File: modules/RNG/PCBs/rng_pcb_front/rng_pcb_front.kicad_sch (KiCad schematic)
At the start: 34 parts, among them J1 THONKICONN, J10 Conn_01x08_Pin, J2 THONKICONN, J3 THONKICONN, J4 THONKICONN, J5 THONKICONN, J6 THONKICONN, J7 Conn_01x07_Pin, J8 Conn_02x03_Socket, J9 Conn_01x06_Pin, SW1 RotaryEncoder_Switch, SW2 TAIWAY 200CWMSP1T3B4M2, SW3 TAIWAY 200CWMSP1T3B4M2

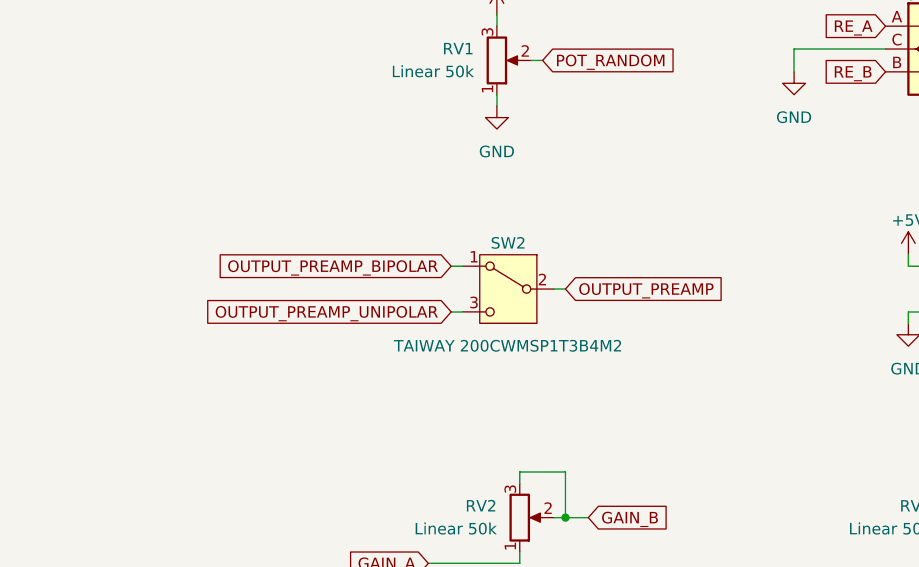
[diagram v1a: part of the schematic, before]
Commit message: update RNG firmware to use new pins
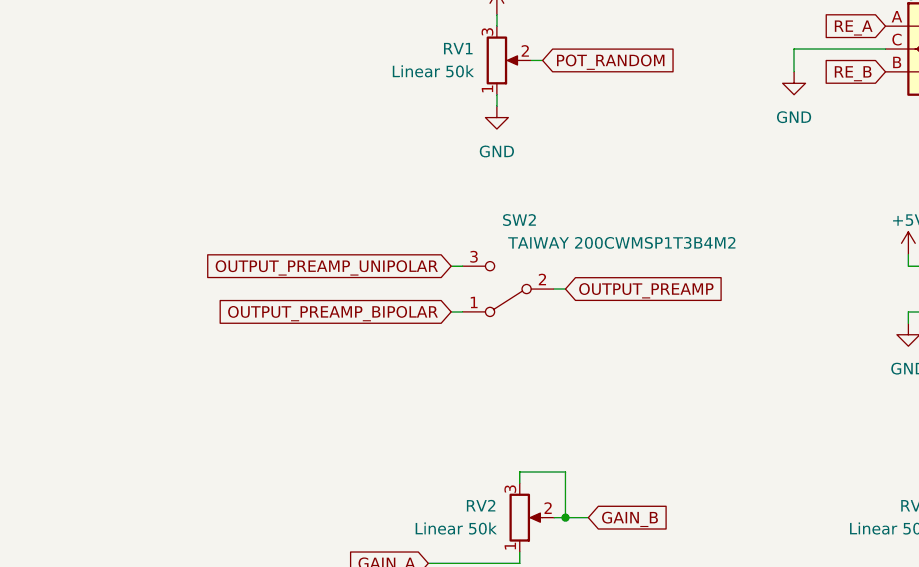
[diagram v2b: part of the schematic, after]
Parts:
- removed SW2: TAIWAY 200CWMSP1T3B4M2, FreeModualr:TAIWAY 200CWMSP1T3B4M2, symbol Switch:SW_SPDT
- added SW2: TAIWAY 200CWMSP1T3B4M2, FreeModualr:TAIWAY 200CWMSP1T3B4M2, symbol FreeModular:SW_SPDT_small
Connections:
- net OUTPUT_PREAMP: now also SW2.2 (B)
- net OUTPUT_PREAMP_BIPOLAR: now also SW2.1 (A)
- net OUTPUT_PREAMP_UNIPOLAR: now also SW2.3 (C)
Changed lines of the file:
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@@
 	(global_label "OUTPUT_PREAMP_UNIPOLAR"
 		(shape input)
-		(at 92.71 106.68 180)
+		(at 92.71 101.6 180)
 		(fields_autoplaced yes)
 		(effects
@@
 		)
 		(property "Intersheetrefs" "${INTERSHEET_REFS}"
-			(at 63.8409 106.68 0)
+			(at 63.8409 101.6 0)
 			(effects
 				(font
@@
 	(global_label "OUTPUT_PREAMP_BIPOLAR"
 		(shape input)
-		(at 92.71 101.6 180)
+		(at 92.71 106.68 180)
 		(fields_autoplaced yes)
 		(effects
@@
 		)
 		(property "Intersheetrefs" "${INTERSHEET_REFS}"
-			(at 65.2319 101.6 0)
+			(at 65.2319 106.68 0)
 			(effects
 				(font
@@
 	)
 	(symbol
+		(lib_id "FreeModular:SW_SPDT_small")
+		(at 99.06 104.14 180)
+		(unit 1)
+		(exclude_from_sim no)
+		(in_bom yes)
+		(on_board yes)
+		(dnp no)
+		(property "Reference" "SW2"
+			(at 100.33 96.52 0)
+			(effects
+				(font
+					(size 1.27 1.27)
+				)
+			)
+		)
+		(property "Value" "TAIWAY 200CWMSP1T3B4M2"
+			(at 111.76 99.06 0)
+			(effects
+				(font
+					(size 1.27 1.27)
+				)
+			)
+		)
+		(property "Footprint" "FreeModualr:TAIWAY 200CWMSP1T3B4M2"
+			(at 99.06 104.14 0)
+			(effects
+				(font
+					(size 1.27 1.27)
+				)
+				(hide yes)
+			)
+		)
+		(property "Datasheet" "https://www.taiway.com/resource/annexes/product_items/81/383d79ce24fd13ac9c4d36337853e90c.pdf"
+			(at 99.06 104.14 0)
+			(effects
+				(font
+					(size 1.27 1.27)
+				)
+				(hide yes)
+			)
+		)
+		(property "Description" ""
+			(at 99.06 104.14 0)
+			(effects
+				(font
+					(size 1.27 1.27)
+				)
+				(hide yes)
+			)
+		)
+		(pin "1"
+		)
+		(pin "2"
+		)
+		(pin "3"
+		)
+		(instances
+			(project "rng_pcb_front"
+				(path "/53c2a808-e337-4b11-8126-cc5e1b54736a"
+					(reference "SW2")
+					(unit 1)
+				)
+			)
+		)
+	)
+	(symbol
 		(lib_id "Device:R")
 		(at 246.38 102.87 90)
@@
 					(unit 1)
 				)
-			)
-		)
-	)
-	(symbol
-		(lib_id "Switch:SW_SPDT")
-		(at 99.06 104.14 0)
-		(mirror y)
-		(unit 1)
-		(exclude_from_sim no)
-		(in_bom yes)
-		(on_board yes)
-		(dnp no)
-		(property "Reference" "SW2"
-			(at 99.06 99.06 0)
-			(effects
-				(font
-					(size 1.27 1.27)
-				)
-			)
-		)
-		(property "Value" "TAIWAY 200CWMSP1T3B4M2"
-			(at 99.06 110.49 0)
-			(effects
-				(font
-					(size 1.27 1.27)
-				)
-			)
-		)
-		(property "Footprint" "FreeModualr:TAIWAY 200CWMSP1T3B4M2"
-			(at 99.06 104.14 0)
-			(effects
-				(font
-					(size 1.27 1.27)
-				)
-				(hide yes)
-			)
-		)
-		(property "Datasheet" "~"
-			(at 99.06 111.76 0)
-			(effects
-				(font
-					(size 1.27 1.27)
-				)
-				(hide yes)
-			)
-		)
-		(property "Description" ""
-			(at 99.06 104.14 0)
-			(effects
-				(font
-					(size 1.27 1.27)
-				)
-				(hide yes)
-			)
-		)
-		(pin "1"
-		)
-		(pin "2"
-		)
-		(pin "3"
-		)
-		(instances
-			(project "rng_pcb_front"
-				(path "/53c2a808-e337-4b11-8126-cc5e1b54736a"
-					(reference "SW2")
-					(unit 1)
-				)

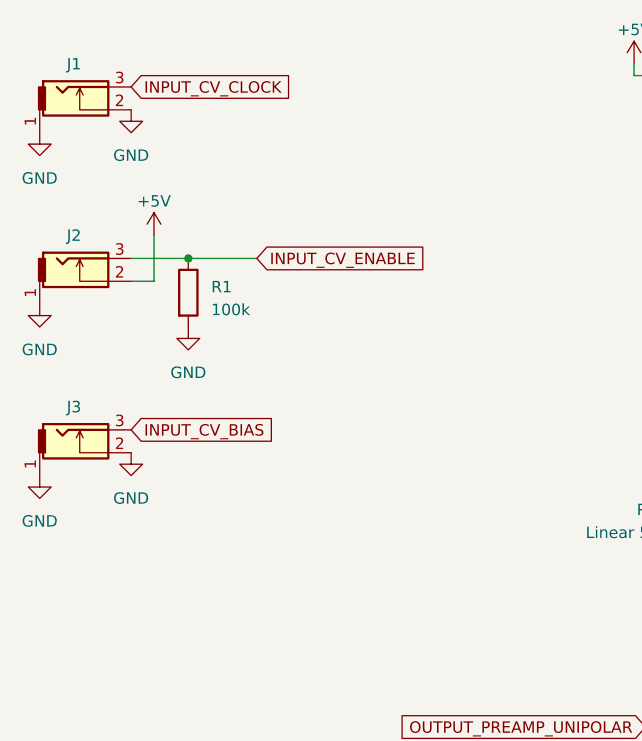
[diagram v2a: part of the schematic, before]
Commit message: add pulldown resistor to RNG clock input
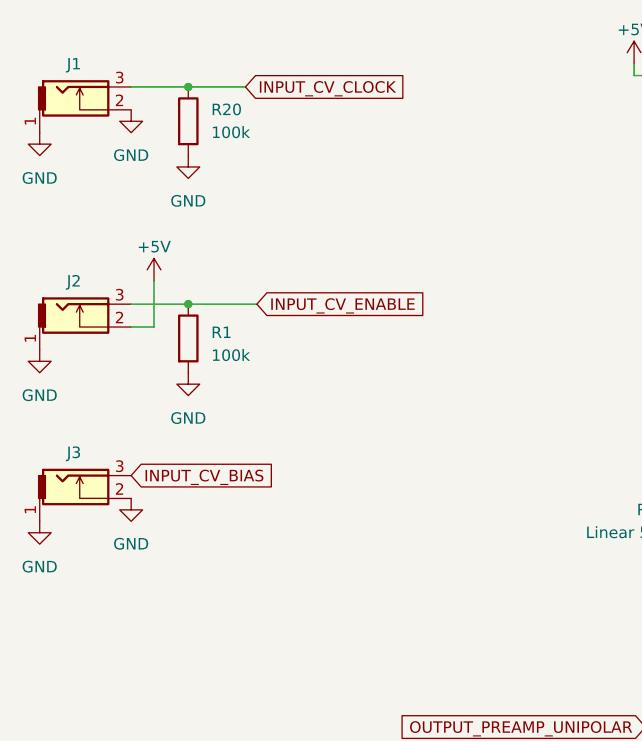
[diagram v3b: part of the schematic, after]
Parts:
- added R20: 100k, Resistor_THT:R_Axial_DIN0207_L6.3mm_D2.5mm_P7.62mm_Horizontal, symbol Device:R
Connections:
- net GND: now also R20.2
- net INPUT_CV_CLOCK: now also R20.1
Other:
- company: (none) -> Free Modular
- title: (none) -> RNG Front
- moved on the sheet: J2, J3, R1

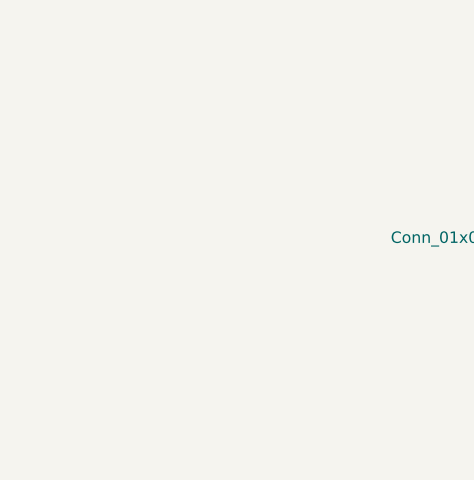
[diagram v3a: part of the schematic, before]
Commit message: Add SMD option for LED driver on RNG
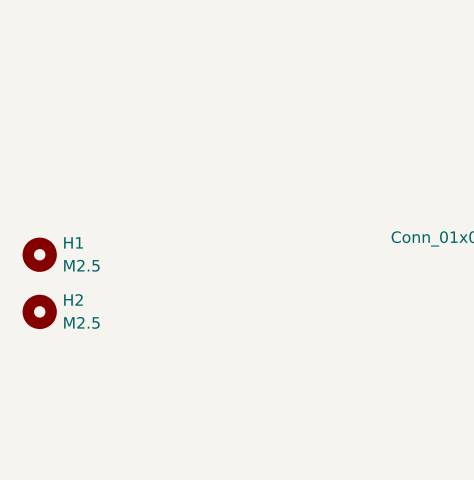
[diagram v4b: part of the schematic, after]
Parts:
- added H1, H2: M2.5, MountingHole:MountingHole_2.7mm_M2.5, symbol Mechanical:MountingHole
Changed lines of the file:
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@@
 	(title_block
 		(title "RNG Front")
-		(date "2024-05-04")
-		(rev "v3.1")
+		(date "2024-09-19")
+		(rev "v3.3")
 		(company "Free Modular")
 	)
@@
 	)
 	(symbol
+		(lib_id "Mechanical:MountingHole")
+		(at 25.4 171.45 0)
+		(unit 1)
+		(exclude_from_sim yes)
+		(in_bom no)
+		(on_board yes)
+		(dnp no)
+		(fields_autoplaced yes)
+		(property "Reference" "H2"
+			(at 27.94 170.1799 0)
+			(effects
+				(font
+					(size 1.27 1.27)
+				)
+				(justify left)
+			)
+		)
+		(property "Value" "M2.5"
+			(at 27.94 172.7199 0)
+			(effects
+				(font
+					(size 1.27 1.27)
+				)
+				(justify left)
+			)
+		)
+		(property "Footprint" "MountingHole:MountingHole_2.7mm_M2.5"
+			(at 25.4 171.45 0)
+			(effects
+				(font
+					(size 1.27 1.27)
+				)
+				(hide yes)
+			)
+		)
+		(property "Datasheet" "~"
+			(at 25.4 171.45 0)
+			(effects
+				(font
+					(size 1.27 1.27)
+				)
+				(hide yes)
+			)
+		)
+		(property "Description" "Mounting Hole without connection"
+			(at 25.4 171.45 0)
+			(effects
+				(font
+					(size 1.27 1.27)
+				)
+				(hide yes)
+			)
+		)
+		(instances
+			(project "rng_pcb_front"
+				(path "/53c2a808-e337-4b11-8126-cc5e1b54736a"
+					(reference "H2")
+					(unit 1)
+				)
+			)
+		)
+	)
+	(symbol
 		(lib_id "FreeModular:THONKICONN")
 		(at 30.48 76.2 0)
@@
 					(unit 1)
 				)
+			)
+		)
+	)
+	(symbol
+		(lib_id "Mechanical:MountingHole")
+		(at 25.4 165.1 0)
+		(unit 1)
+		(exclude_from_sim yes)
+		(in_bom no)
+		(on_board yes)
+		(dnp no)
+		(fields_autoplaced yes)
+		(property "Reference" "H1"
+			(at 27.94 163.8299 0)
+			(effects
+				(font
+					(size 1.27 1.27)
+				)
+				(justify left)
+			)
+		)
+		(property "Value" "M2.5"
+			(at 27.94 166.3699 0)
+			(effects
+				(font
+					(size 1.27 1.27)
+				)
+				(justify left)
+			)
+		)
+		(property "Footprint" "MountingHole:MountingHole_2.7mm_M2.5"
+			(at 25.4 165.1 0)
+			(effects
+				(font
+					(size 1.27 1.27)
+				)
+				(hide yes)
+			)
+		)
+		(property "Datasheet" "~"
+			(at 25.4 165.1 0)
+			(effects
+				(font
+					(size 1.27 1.27)
+				)
+				(hide yes)
+			)
+		)
+		(property "Description" "Mounting Hole without connection"
+			(at 25.4 165.1 0)
+			(effects
+				(font
+					(size 1.27 1.27)
+				)
+				(hide yes)
+			)
+		)
+		(instances
+			(project "rng_pcb_front"
+				(path "/53c2a808-e337-4b11-8126-cc5e1b54736a"
+					(reference "H1")
+					(unit 1)
+				)

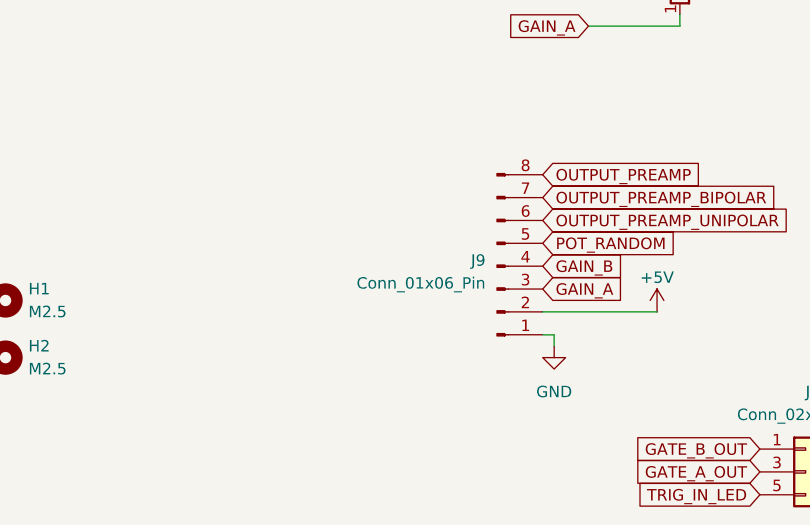
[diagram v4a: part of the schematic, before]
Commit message: Update kicad files to reflect 8-pin connections instead of 6-pin.
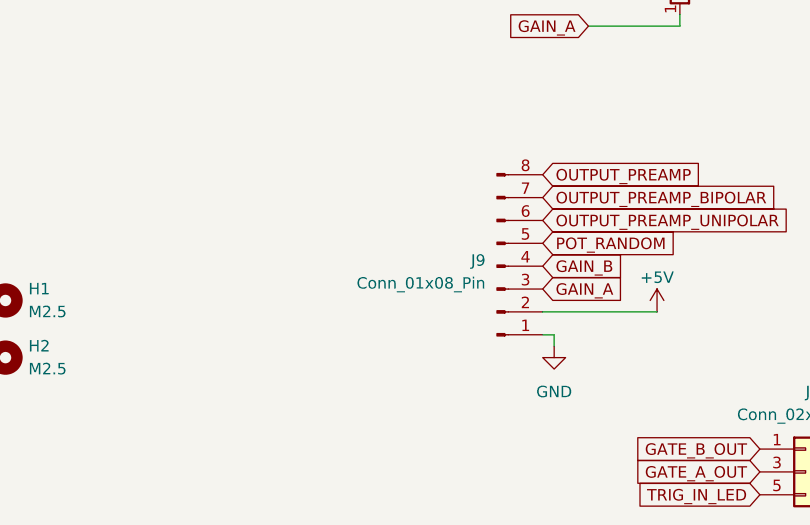
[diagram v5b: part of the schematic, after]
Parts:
- J9: value Conn_01x06_Pin -> Conn_01x08_Pin
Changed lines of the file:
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@@
 			)
 		)
-		(property "Value" "Conn_01x06_Pin"
+		(property "Value" "Conn_01x08_Pin"
 			(at 78.74 163.195 0)
 			(effects
